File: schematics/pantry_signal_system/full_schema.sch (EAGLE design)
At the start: 78 parts, among them J1 JST-XH254-2P, J2 JST-XH254-3P, J3 JST-XH254-2P, J4 JST-XH254-3P, J5 JST-XH254-2P, J6 JST-XH254-2P, J7 JST-XH254-2P, J8 JST-XH254-2P, Q1 STP14NM50N, Q12 STP14NM50N, Q13 STP14NM50N, Q14 2N3904, Q2 STP14NM50N, Q7 2N3904, Q8 2N3904, Q9 STP14NM50N, SW1 SWITCH, SW2 SWITCH, U1 MCP1703T-5002E/CB, U10 FAN73611, U11 FAN73611, U2 AD8544, U3 ATTINY13, U4 ATMEGA328P, U5 MCP1703T-5002E/CB, U6 I2C_DISPLAY, U7 BME280BME280-CONNECTOR-ONLY, U8 E220-900T22D, U9 FAN73611

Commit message: Air drier schema works
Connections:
- removed net USE_PRIMARY_BATTERY_OFFSET: D3.P$1, Q1.S, U9.VS
- removed net USE_RESERVE_BATTERY_OFFSET: D4.P$1, Q2.S, U10.VS
- new net N$12: D3.P$1, Q1.S
- new net N$13: D4.P$1, Q2.S
- net GND: now also U10.VS, U11.VS, U9.VS
- net N$4: no longer U11.VS

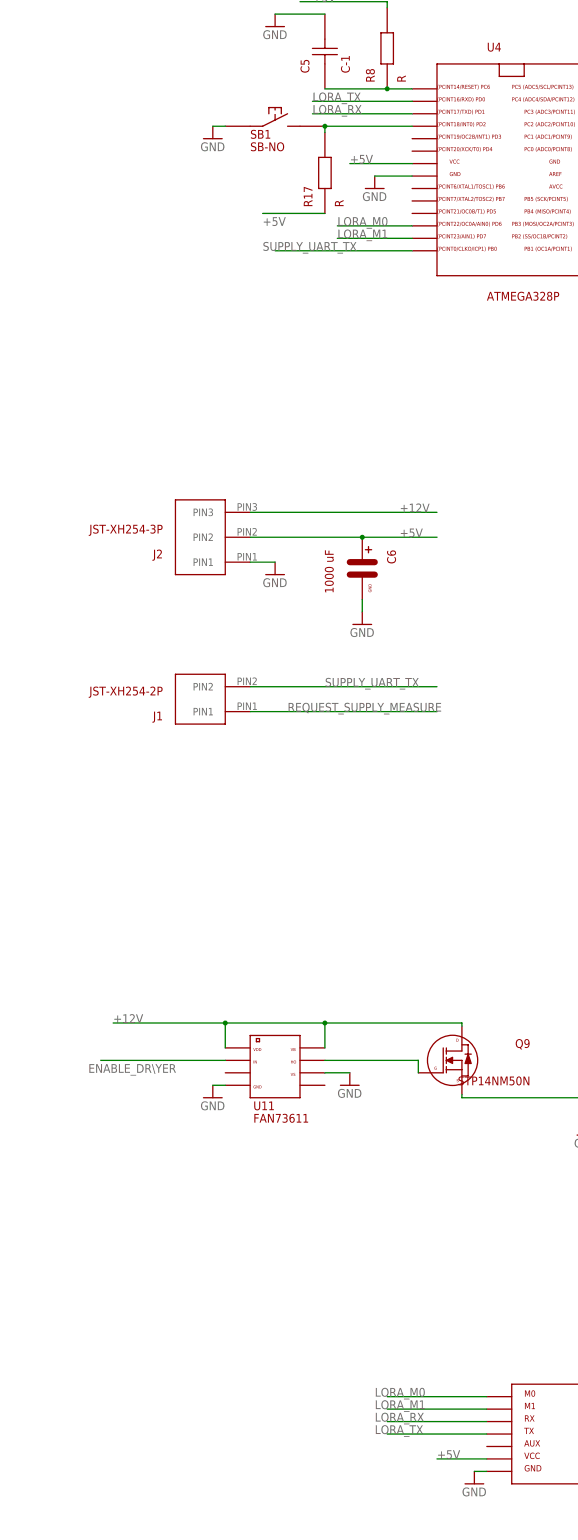
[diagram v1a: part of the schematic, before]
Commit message: Lora module FW and HW works. Encrypted connection betweed modules estabilished
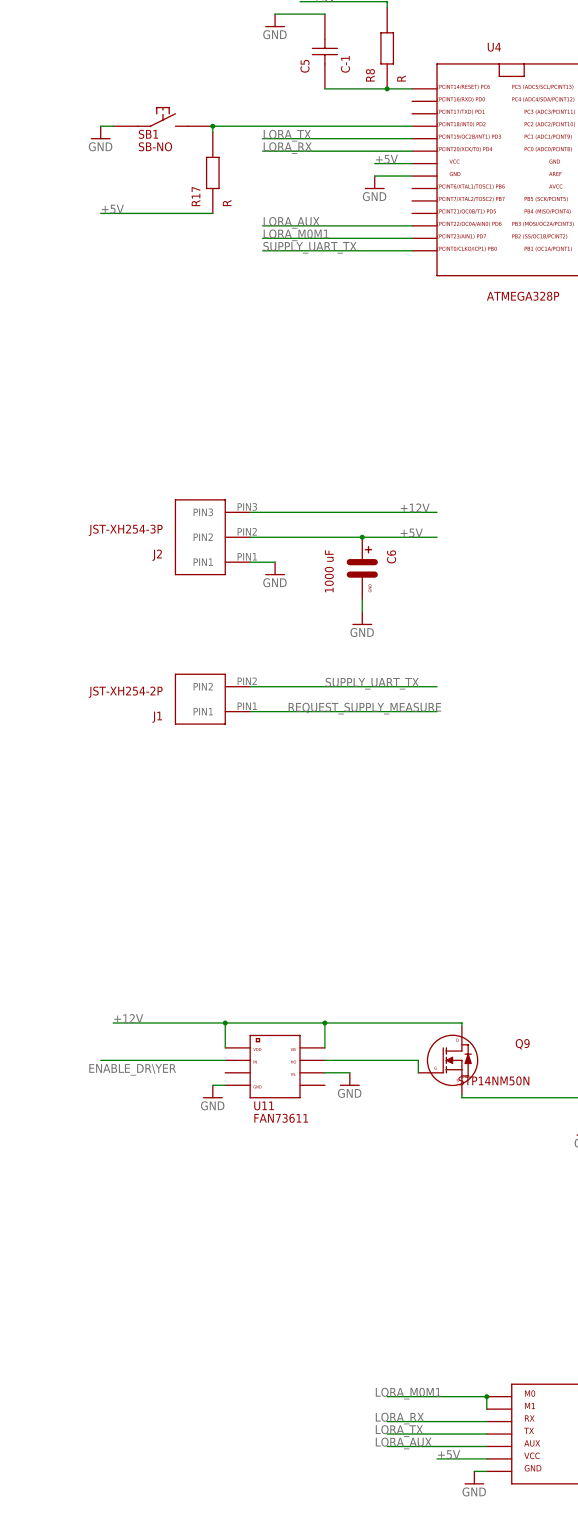
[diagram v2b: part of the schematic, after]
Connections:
- removed net LORA_M0: U4.PD6, U8.M0
- removed net LORA_M1: U4.PD7, U8.M1
- new net LORA_AUX: U4.PD6, U8.AUX
- new net LORA_M0M1: U4.PD7, U8.M0, U8.M1
- net LORA_RX: now also U4.PD4; no longer U4.PD1
- net LORA_TX: now also U4.PD3; no longer U4.PD0
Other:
- moved on the sheet: R17, SB1

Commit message: Added firmware for supply module (not tested yet)
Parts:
- added C4: 0.1 uF, my_devices:C-1
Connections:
- net GND: now also C4.P$2
- net IS_USE_RESERVE_BATTERY: now also U3.PB4; no longer U3.PB0
- net N$9: now also C4.P$1
- net SUPPLY_UART_TX: now also U3.PB0; no longer U3.PB4
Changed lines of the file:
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@@
 <part name="GND38" library="supply1" library_urn="urn:adsk.eagle:library:371" deviceset="GND" device=""/>
 <part name="GND39" library="supply1" library_urn="urn:adsk.eagle:library:371" deviceset="GND" device=""/>
+<part name="C4" library="my_devices" deviceset="C-1" device="" value="0.1 uF"/>
+<part name="GND40" library="supply1" library_urn="urn:adsk.eagle:library:371" deviceset="GND" device=""/>
 </parts>
 <sheets>
@@
 <attribute name="VALUE" x="99.06" y="-99.06" size="1.778" layer="96"/>
 </instance>
+<instance part="C4" gate="G$1" x="347.98" y="35.56" smashed="yes" grouprefs="SUPPLY_AVR">
+<attribute name="NAME" x="343.535" y="38.735" size="1.778" layer="94"/>
+<attribute name="VALUE" x="343.535" y="30.48" size="1.778" layer="94"/>
+</instance>
+<instance part="GND40" gate="1" x="358.14" y="33.02" smashed="yes" grouprefs="SUPPLY_AVR">
+<attribute name="VALUE" x="355.6" y="30.48" size="1.778" layer="96"/>
+</instance>
 </instances>
 <busses>
@@
 <pinref part="GND39" gate="1" pin="GND"/>
 <wire x1="96.52" y1="-93.98" x2="101.6" y2="-93.98" width="0.1524" layer="91" grouprefs="DISCHARGE_CONTROL_AND_POWER_SWITCH"/>
+</segment>
+<segment>
+<pinref part="C4" gate="G$1" pin="P$2"/>
+<pinref part="GND40" gate="1" pin="GND"/>
+<wire x1="355.6" y1="35.56" x2="358.14" y2="35.56" width="0.1524" layer="91" grouprefs="SUPPLY_AVR"/>
 </segment>
 </net>
@@
 </segment>
 <segment>
-<pinref part="U3" gate="G$1" pin="PB0"/>
-<wire x1="323.215" y1="27.94" x2="345.44" y2="27.94" width="0.1524" layer="91" grouprefs="SUPPLY_AVR"/>
-<label x="325.12" y="27.94" size="1.778" layer="95" grouprefs="SUPPLY_AVR"/>
-</segment>
-<segment>
 <pinref part="U10" gate="G$1" pin="IN"/>
 <wire x1="76.2" y1="-91.44" x2="50.8" y2="-91.44" width="0.1524" layer="91" grouprefs="DISCHARGE_CONTROL_AND_POWER_SWITCH"/>
 <label x="45.72" y="-91.44" size="1.778" layer="95" grouprefs="DISCHARGE_CONTROL_AND_POWER_SWITCH"/>
+</segment>
+<segment>
+<pinref part="U3" gate="G$1" pin="PB4"/>
+<wire x1="287.655" y1="30.48" x2="264.16" y2="30.48" width="0.1524" layer="91" grouprefs="SUPPLY_AVR"/>
+<label x="256.54" y="30.48" size="1.778" layer="95" grouprefs="SUPPLY_AVR"/>
 </segment>
 </net>
@@
 </segment>
 <segment>
-<pinref part="U3" gate="G$1" pin="PB4"/>
-<wire x1="287.655" y1="30.48" x2="264.16" y2="30.48" width="0.1524" layer="91" grouprefs="SUPPLY_AVR"/>
-<label x="264.16" y="30.48" size="1.778" layer="95" grouprefs="SUPPLY_AVR"/>
+<pinref part="U3" gate="G$1" pin="PB0"/>
+<wire x1="323.215" y1="27.94" x2="323.215" y2="22.86" width="0.1524" layer="91" grouprefs="SUPPLY_AVR"/>
+<wire x1="323.215" y1="22.86" x2="345.44" y2="22.86" width="0.1524" layer="91" grouprefs="SUPPLY_AVR"/>
+<label x="327.66" y="22.86" size="1.778" layer="95" grouprefs="SUPPLY_AVR"/>
 </segment>
 </net>
@@
 <net name="N$21" class="0">
 <segment>
-<wire x1="779.78" y1="137.16" x2="782.32" y2="137.16" width="0.1524" layer="91"/>
 <wire x1="782.32" y1="137.16" x2="782.32" y2="-266.7" width="0.1524" layer="91" style="shortdash"/>
 </segment>
@@
 <pinref part="Q7" gate="G$1" pin="E"/>
 <wire x1="323.215" y1="35.56" x2="327.66" y2="35.56" width="0.1524" layer="91" grouprefs="SUPPLY_AVR"/>
+<pinref part="C4" gate="G$1" pin="P$1"/>
+<wire x1="327.66" y1="35.56" x2="340.36" y2="35.56" width="0.1524" layer="91" grouprefs="SUPPLY_AVR"/>
+<junction x="327.66" y="35.56" grouprefs="SUPPLY_AVR"/>
 </segment>
 </net>
@@
 <segment>
 <pinref part="U3" gate="G$1" pin="PB1"/>
-<wire x1="323.215" y1="30.48" x2="345.44" y2="30.48" width="0.1524" layer="91" grouprefs="SUPPLY_AVR"/>
-<label x="325.12" y="30.48" size="1.778" layer="95" grouprefs="SUPPLY_AVR"/>
+<wire x1="323.215" y1="30.48" x2="325.12" y2="30.48" width="0.1524" layer="91" grouprefs="SUPPLY_AVR"/>
+<wire x1="325.12" y1="30.48" x2="325.12" y2="25.4" width="0.1524" layer="91" grouprefs="SUPPLY_AVR"/>
+<wire x1="325.12" y1="25.4" x2="350.52" y2="25.4" width="0.1524" layer="91" grouprefs="SUPPLY_AVR"/>
+<label x="327.66" y="25.4" size="1.778" layer="95" grouprefs="SUPPLY_AVR"/>
 </segment>
 </net>
@@
 <segment>
 <pinref part="U3" gate="G$1" pin="PB2"/>
-<wire x1="323.215" y1="33.02" x2="345.44" y2="33.02" width="0.1524" layer="91" grouprefs="SUPPLY_AVR"/>
-<label x="325.12" y="33.02" size="1.778" layer="95" grouprefs="SUPPLY_AVR"/>
-</segment>
-</net>
+<wire x1="323.215" y1="33.02" x2="327.66" y2="33.02" width="0.1524" layer="91" grouprefs="SUPPLY_AVR"/>
+<wire x1="327.66" y1="33.02" x2="327.66" y2="27.94" width="0.1524" layer="91" grouprefs="SUPPLY_AVR"/>
+<wire x1="327.66" y1="27.94" x2="350.52" y2="27.94" width="0.1524" layer="91" grouprefs="SUPPLY_AVR"/>
+<label x="330.2" y="27.94" size="1.778" layer="95" grouprefs="SUPPLY_AVR"/>
+</segment>
+</net>

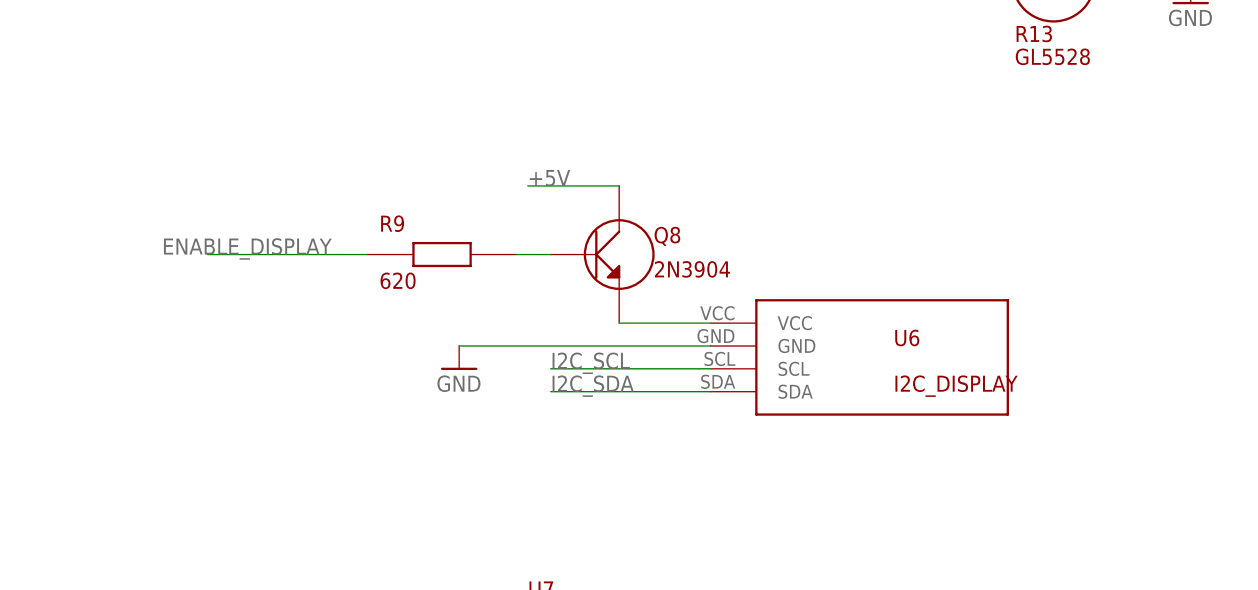
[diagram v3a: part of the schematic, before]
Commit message: Display driver and schema ready
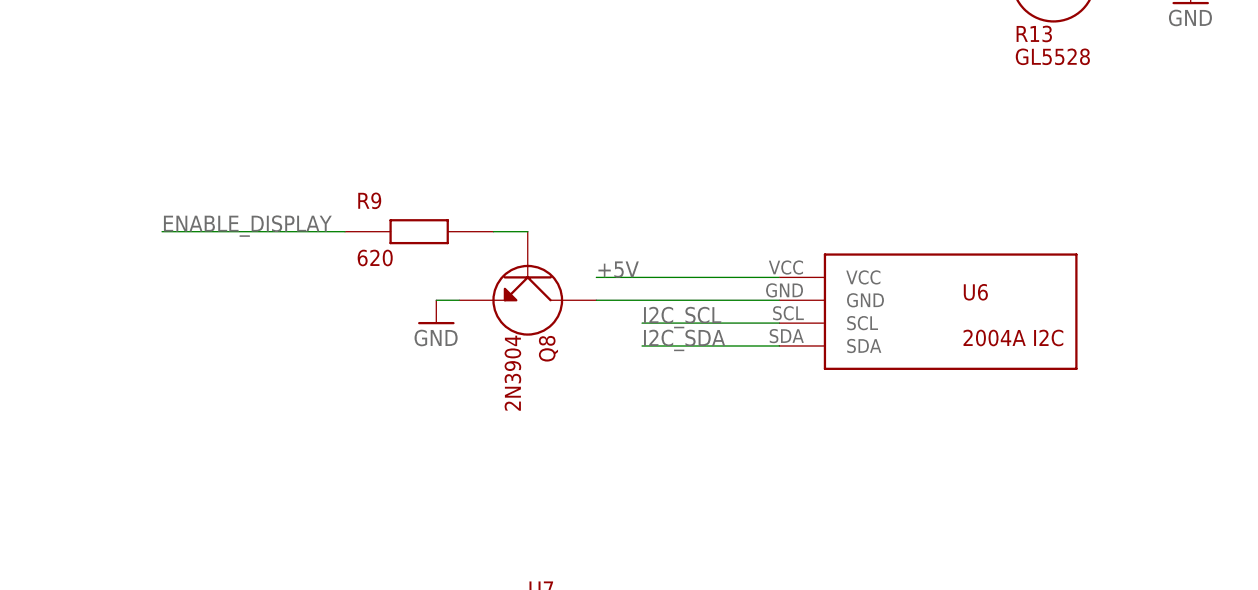
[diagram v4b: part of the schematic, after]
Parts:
- U6: value I2C_DISPLAY -> 2004A I2C
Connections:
- net +5V: now also U6.VCC; no longer Q8.C
- net GND: now also Q8.E; no longer U6.GND
- net N$10: now also Q8.C, U6.GND; no longer Q8.E, U6.VCC
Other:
- moved on the sheet: Q8, R9, U6
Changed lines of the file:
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@@
 <part name="GND20" library="supply1" library_urn="urn:adsk.eagle:library:371" deviceset="GND" device=""/>
 <part name="R8" library="my_devices" deviceset="R" device=""/>
-<part name="U6" library="my_devices" deviceset="I2C_DISPLAY" device=""/>
-<part name="GND21" library="supply1" library_urn="urn:adsk.eagle:library:371" deviceset="GND" device=""/>
+<part name="U6" library="my_devices" deviceset="I2C_DISPLAY" device="" value="2004A I2C"/>
 <part name="Q8" library="my_devices" deviceset="TRANSISTOR_NPN" device="" value="2N3904"/>
-<part name="R9" library="my_devices" deviceset="R" device="" value="620"/>
 <part name="C6" library="my_devices" deviceset="C" device="" value="1000 uF"/>
 <part name="GND22" library="supply1" library_urn="urn:adsk.eagle:library:371" deviceset="GND" device=""/>
@@
 <part name="C4" library="my_devices" deviceset="C-1" device="" value="0.1 uF"/>
 <part name="GND40" library="supply1" library_urn="urn:adsk.eagle:library:371" deviceset="GND" device=""/>
+<part name="GND21" library="supply1" library_urn="urn:adsk.eagle:library:371" deviceset="GND" device=""/>
+<part name="R9" library="my_devices" deviceset="R" device="" value="620"/>
 </parts>
 <sheets>
@@
 <attribute name="VALUE" x="519.43" y="46.99" size="1.778" layer="94" rot="R90"/>
 </instance>
-<instance part="U6" gate="G$1" x="629.92" y="-66.04" smashed="yes" grouprefs="DISPLAY">
-<attribute name="NAME" x="645.16" y="-66.04" size="1.778" layer="94"/>
-<attribute name="VALUE" x="645.16" y="-71.12" size="1.778" layer="94"/>
-</instance>
-<instance part="GND21" gate="1" x="596.9" y="-68.58" smashed="yes" grouprefs="DISPLAY">
-<attribute name="VALUE" x="594.36" y="-71.12" size="1.778" layer="96"/>
-</instance>
-<instance part="Q8" gate="G$1" x="614.68" y="-55.88" smashed="yes" grouprefs="DISPLAY">
-<attribute name="NAME" x="618.49" y="-54.61" size="1.778" layer="94"/>
-<attribute name="VALUE" x="618.49" y="-58.42" size="1.778" layer="94"/>
-</instance>
-<instance part="R9" gate="G$1" x="594.36" y="-55.88" smashed="yes" grouprefs="DISPLAY">
-<attribute name="NAME" x="588.01" y="-53.34" size="1.778" layer="94"/>
-<attribute name="VALUE" x="588.01" y="-59.69" size="1.778" layer="94"/>
+<instance part="U6" gate="G$1" x="637.54" y="-60.96" smashed="yes" grouprefs="DISPLAY">
+<attribute name="NAME" x="652.78" y="-60.96" size="1.778" layer="94"/>
+<attribute name="VALUE" x="652.78" y="-66.04" size="1.778" layer="94"/>
+</instance>
+<instance part="Q8" gate="G$1" x="604.52" y="-60.96" smashed="yes" rot="R270" grouprefs="DISPLAY">
+<attribute name="NAME" x="605.79" y="-64.77" size="1.778" layer="94" rot="R270"/>
+<attribute name="VALUE" x="601.98" y="-64.77" size="1.778" layer="94" rot="R270"/>
 </instance>
 <instance part="C6" gate="G$1" x="510.54" y="-53.34" smashed="yes" rot="R270" grouprefs="LOGIC_BLOCK_CONNECTORS">
@@
 <instance part="GND40" gate="1" x="358.14" y="33.02" smashed="yes" grouprefs="SUPPLY_AVR">
 <attribute name="VALUE" x="355.6" y="30.48" size="1.778" layer="96"/>
+</instance>
+<instance part="GND21" gate="1" x="594.36" y="-63.5" smashed="yes" grouprefs="DISPLAY">
+<attribute name="VALUE" x="591.82" y="-66.04" size="1.778" layer="96"/>
+</instance>
+<instance part="R9" gate="G$1" x="591.82" y="-53.34" smashed="yes" grouprefs="DISPLAY">
+<attribute name="NAME" x="585.47" y="-50.8" size="1.778" layer="94"/>
+<attribute name="VALUE" x="585.47" y="-57.15" size="1.778" layer="94"/>
 </instance>
 </instances>
@@
 </segment>
 <segment>
-<pinref part="U6" gate="G$1" pin="GND"/>
-<wire x1="624.84" y1="-66.04" x2="596.9" y2="-66.04" width="0.1524" layer="91" grouprefs="DISPLAY"/>
-<pinref part="GND21" gate="1" pin="GND"/>
-</segment>
-<segment>
 <pinref part="C6" gate="G$1" pin="PIN_GND"/>
 <pinref part="GND22" gate="1" pin="GND"/>
@@
 <pinref part="GND40" gate="1" pin="GND"/>
 <wire x1="355.6" y1="35.56" x2="358.14" y2="35.56" width="0.1524" layer="91" grouprefs="SUPPLY_AVR"/>
+</segment>
+<segment>
+<pinref part="Q8" gate="G$1" pin="E"/>
+<pinref part="GND21" gate="1" pin="GND"/>
+<wire x1="596.9" y1="-60.96" x2="594.36" y2="-60.96" width="0.1524" layer="91" grouprefs="DISPLAY"/>
 </segment>
 </net>
@@
 </segment>
 <segment>
-<pinref part="Q8" gate="G$1" pin="C"/>
-<wire x1="614.68" y1="-48.26" x2="604.52" y2="-48.26" width="0.1524" layer="91" grouprefs="DISPLAY"/>
-<label x="604.52" y="-48.26" size="1.778" layer="95" grouprefs="DISPLAY"/>
-</segment>
-<segment>
 <pinref part="U7" gate="G$1" pin="VCC"/>
 <wire x1="589.28" y1="-99.06" x2="576.58" y2="-99.06" width="0.1524" layer="91" grouprefs="TEMPERATURE_AND_HUMIDITY_SENSOR"/>
@@
 <wire x1="327.66" y1="50.8" x2="358.14" y2="50.8" width="0.1524" layer="91" grouprefs="SUPPLY_AVR"/>
 <label x="353.06" y="48.26" size="1.778" layer="95" grouprefs="SUPPLY_AVR"/>
+</segment>
+<segment>
+<pinref part="U6" gate="G$1" pin="VCC"/>
+<wire x1="632.46" y1="-58.42" x2="612.14" y2="-58.42" width="0.1524" layer="91" grouprefs="DISPLAY"/>
+<label x="612.14" y="-58.42" size="1.778" layer="95" grouprefs="DISPLAY"/>
 </segment>
 </net>
@@
 </segment>
 <segment>
-<pinref part="U6" gate="G$1" pin="SDA"/>
-<wire x1="624.84" y1="-71.12" x2="607.06" y2="-71.12" width="0.1524" layer="91" grouprefs="DISPLAY"/>
-<label x="607.06" y="-71.12" size="1.778" layer="95" grouprefs="DISPLAY"/>
-</segment>
-<segment>
 <pinref part="U7" gate="G$1" pin="SDA"/>
 <wire x1="589.28" y1="-106.68" x2="571.5" y2="-106.68" width="0.1524" layer="91" grouprefs="TEMPERATURE_AND_HUMIDITY_SENSOR"/>
 <label x="571.5" y="-106.68" size="1.778" layer="95" grouprefs="TEMPERATURE_AND_HUMIDITY_SENSOR"/>
 </segment>
+<segment>
+<pinref part="U6" gate="G$1" pin="SDA"/>
+<wire x1="632.46" y1="-66.04" x2="617.22" y2="-66.04" width="0.1524" layer="91" grouprefs="DISPLAY"/>
+<label x="617.22" y="-66.04" size="1.778" layer="95" grouprefs="DISPLAY"/>
+</segment>
 </net>
 <net name="I2C_SCL" class="0">
@@
 </segment>
 <segment>
-<pinref part="U6" gate="G$1" pin="SCL"/>
-<wire x1="624.84" y1="-68.58" x2="607.06" y2="-68.58" width="0.1524" layer="91" grouprefs="DISPLAY"/>
-<label x="607.06" y="-68.58" size="1.778" layer="95" grouprefs="DISPLAY"/>
-</segment>
-<segment>
 <pinref part="U7" gate="G$1" pin="SCL"/>
 <wire x1="589.28" y1="-104.14" x2="571.5" y2="-104.14" width="0.1524" layer="91" grouprefs="TEMPERATURE_AND_HUMIDITY_SENSOR"/>
 <label x="571.5" y="-104.14" size="1.778" layer="95" grouprefs="TEMPERATURE_AND_HUMIDITY_SENSOR"/>
 </segment>
-</net>
-<net name="N$10" class="0">
-<segment>
-<pinref part="U6" gate="G$1" pin="VCC"/>
-<pinref part="Q8" gate="G$1" pin="E"/>
-<wire x1="624.84" y1="-63.5" x2="614.68" y2="-63.5" width="0.1524" layer="91" grouprefs="DISPLAY"/>
+<segment>
+<pinref part="U6" gate="G$1" pin="SCL"/>
+<wire x1="632.46" y1="-63.5" x2="617.22" y2="-63.5" width="0.1524" layer="91" grouprefs="DISPLAY"/>
+<label x="617.22" y="-63.5" size="1.778" layer="95" grouprefs="DISPLAY"/>
 </segment>
 </net>
@@
 <segment>
 <pinref part="R9" gate="G$1" pin="P$1"/>
-<wire x1="586.74" y1="-55.88" x2="568.96" y2="-55.88" width="0.1524" layer="91" grouprefs="DISPLAY"/>
-<label x="563.88" y="-55.88" size="1.778" layer="95" grouprefs="DISPLAY"/>
-</segment>
-</net>
-<net name="N$11" class="0">
-<segment>
-<pinref part="Q8" gate="G$1" pin="B"/>
-<pinref part="R9" gate="G$1" pin="P$2"/>
-<wire x1="607.06" y1="-55.88" x2="603.25" y2="-55.88" width="0.1524" layer="91" grouprefs="DISPLAY"/>
+<wire x1="584.2" y1="-53.34" x2="563.88" y2="-53.34" width="0.1524" layer="91" grouprefs="DISPLAY"/>
+<label x="563.88" y="-53.34" size="1.778" layer="95" grouprefs="DISPLAY"/>
 </segment>
 </net>
@@
 </segment>
 </net>
+<net name="N$10" class="0">
+<segment>
+<pinref part="U6" gate="G$1" pin="GND"/>
+<wire x1="612.14" y1="-60.96" x2="632.46" y2="-60.96" width="0.1524" layer="91" grouprefs="DISPLAY"/>
+<pinref part="Q8" gate="G$1" pin="C"/>
+</segment>
+</net>
+<net name="N$11" class="0">
+<segment>
+<pinref part="Q8" gate="G$1" pin="B"/>
+<pinref part="R9" gate="G$1" pin="P$2"/>
+<wire x1="604.52" y1="-53.34" x2="600.71" y2="-53.34" width="0.1524" layer="91" grouprefs="DISPLAY"/>
+</segment>
+</net>
